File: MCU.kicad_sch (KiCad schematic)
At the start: 41 parts, among them IC6 ATSAMD21G18A-MF, J10 Conn_01x10, J11 Conn_01x06, J7 Conn_01x08, J9 Conn_01x08, Q1 XTAL_32.768KHZ_ABRACON_ABS09-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

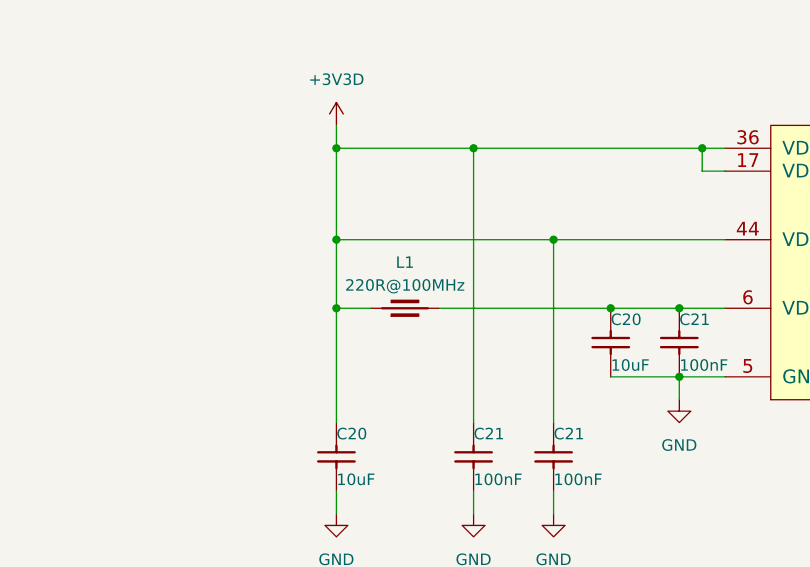
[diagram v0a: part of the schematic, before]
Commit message: Added input connector, switch, filtering and USB TVS
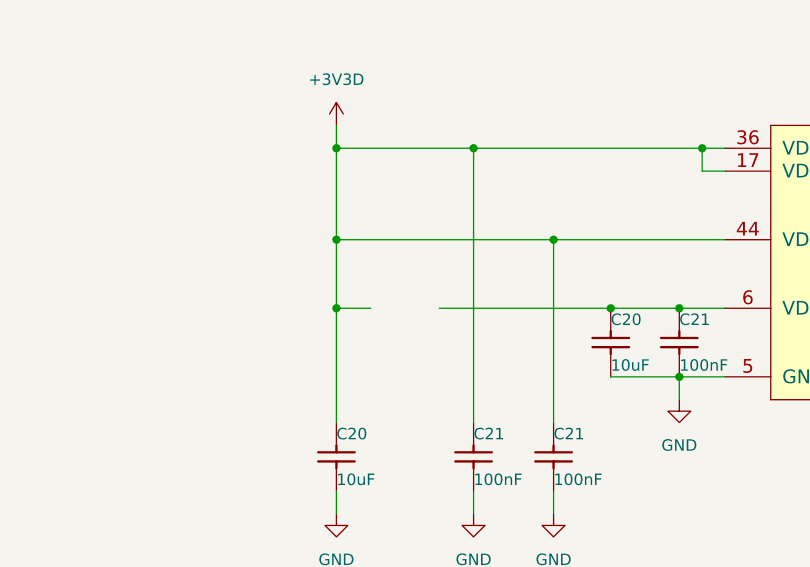
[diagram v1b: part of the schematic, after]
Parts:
- removed L1: IND0603_MURATA_BLM18SG221TN1, Inductors SMD:INDC1608X95N, symbol Inductors SMD:IND0603_MURATA_BLM18SG221TN1
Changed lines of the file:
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@@
-    )
-  )
-  (symbol (lib_id "Inductors SMD:IND0603_MURATA_BLM18SG221TN1") (at 99.06 214.63 0) (unit 1)
-    (in_bom yes) (on_board yes) (dnp no)
-    (property "Reference" "L1" (at 102.87 209.55 0)
-      (effects (font (size 1.27 1.27)))
-    )
-    (property "Value" "IND0603_MURATA_BLM18SG221TN1" (at 99.06 219.583 0)
-      (effects (font (size 1.27 1.27)) (justify left) hide)
-    )
-    (property "Footprint" "Inductors SMD:INDC1608X95N" (at 99.06 221.488 0)
-      (effects (font (size 1.27 1.27)) (justify left) hide)
-    )
-    (property "Datasheet" "\\\\cern.ch\\dfs\\Applications\\Altium\\Datasheets\\IND0603_MURATA_BLM18S.pdf" (at 99.06 223.393 0)
-      (effects (font (size 1.27 1.27)) (justify left) hide)
-    )
-    (property "Val" "220R@100MHz" (at 102.87 212.09 0)
-      (effects (font (size 1.27 1.27)))
-    )
-    (property "Part Number" "IND0603_MURATA_BLM18SG221TN1" (at 99.06 225.298 0)
-      (effects (font (size 1.27 1.27)) (justify left) hide)
-    )
-    (property "Library Ref" "Ferrite Bead" (at 99.06 227.203 0)
-      (effects (font (size 1.27 1.27)) (justify left) hide)
-    )
-    (property "Library Path" "SchLib\\Inductors & Transformers.SchLib" (at 99.06 229.108 0)
-      (effects (font (size 1.27 1.27)) (justify left) hide)
-    )
-    (property "Comment" "220R@100MHz" (at 99.06 231.013 0)
-      (effects (font (size 1.27 1.27)) (justify left) hide)
-    )
-    (property "Component Kind" "Standard" (at 99.06 232.918 0)
-      (effects (font (size 1.27 1.27)) (justify left) hide)
-    )
-    (property "Component Type" "Standard" (at 99.06 234.823 0)
-      (effects (font (size 1.27 1.27)) (justify left) hide)
-    )
-    (property "PackageDescription" " " (at 99.06 236.728 0)
-      (effects (font (size 1.27 1.27)) (justify left) hide)
-    )
-    (property "Pin Count" "2" (at 99.06 238.633 0)
-      (effects (font (size 1.27 1.27)) (justify left) hide)
-    )
-    (property "Footprint Path" "PcbLib\\Inductors SMD.PcbLib" (at 99.06 240.538 0)
-      (effects (font (size 1.27 1.27)) (justify left) hide)
-    )
-    (property "Footprint Ref" "INDC1608X95N" (at 99.06 242.443 0)
-      (effects (font (size 1.27 1.27)) (justify left) hide)
-    )
-    (property "Status" " " (at 99.06 244.348 0)
-      (effects (font (size 1.27 1.27)) (justify left) hide)
-    )
-    (property "Power" "2.5A" (at 99.06 246.253 0)
-      (effects (font (size 1.27 1.27)) (justify left) hide)
-    )
-    (property "Resistance" "0.04R" (at 99.06 248.158 0)
-      (effects (font (size 1.27 1.27)) (justify left) hide)
-    )
-    (property "Tolerance" "±25%" (at 99.06 250.063 0)
-      (effects (font (size 1.27 1.27)) (justify left) hide)
-    )
-    (property "Part Description" "SMD EMIFIL Suppression Chip Ferrite Bead" (at 99.06 251.968 0)
-      (effects (font (size 1.27 1.27)) (justify left) hide)
-    )
-    (property "Manufacturer" "MURATA" (at 99.06 253.873 0)
-      (effects (font (size 1.27 1.27)) (justify left) hide)
-    )
-    (property "Manufacturer Part Number" "BLM18SG221TN1" (at 99.06 255.778 0)
-      (effects (font (size 1.27 1.27)) (justify left) hide)
-    )
-    (property "Case" "0603" (at 99.06 257.683 0)
-      (effects (font (size 1.27 1.27)) (justify left) hide)
-    )
-    (property "Mounted" "Yes" (at 99.06 259.588 0)
-      (effects (font (size 1.27 1.27)) (justify left) hide)
-    )
-    (property "Socket" "No" (at 99.06 261.493 0)
-      (effects (font (size 1.27 1.27)) (justify left) hide)
-    )
-    (property "SMD" "Yes" (at 99.06 263.398 0)
-      (effects (font (size 1.27 1.27)) (justify left) hide)
-    )
-    (property "Sense Comment" " " (at 99.06 265.303 0)
-      (effects (font (size 1.27 1.27)) (justify left) hide)
-    )
-    (property "Sense" "No" (at 99.06 267.208 0)
-      (effects (font (size 1.27 1.27)) (justify left) hide)
-    )
-    (property "Status Comment" " " (at 99.06 269.113 0)
-      (effects (font (size 1.27 1.27)) (justify left) hide)
-    )
-    (property "ComponentHeight" "0.95mm" (at 99.06 271.018 0)
-      (effects (font (size 1.27 1.27)) (justify left) hide)
-    )
-    (property "HelpURL" "\\\\cern.ch\\dfs\\Applications\\Altium\\Datasheets\\IND0603_MURATA_BLM18S.pdf" (at 99.06 272.923 0)
-      (effects (font (size 1.27 1.27)) (justify left) hide)
-    )
-    (property "Author" "CERN DEM MR" (at 99.06 274.828 0)
-      (effects (font (size 1.27 1.27)) (justify left) hide)
-    )
-    (property "CreateDate" "01/08/16 00:00:00" (at 99.06 276.733 0)
-      (effects (font (size 1.27 1.27)) (justify left) hide)
-    )
-    (property "LatestRevisionDate" "10/25/18 00:00:00" (at 99.06 278.638 0)
-      (effects (font (size 1.27 1.27)) (justify left) hide)
-    )
-    (property "Database Table Name" "Inductors & Transformers" (at 99.06 280.543 0)
-      (effects (font (size 1.27 1.27)) (justify left) hide)
-    )
-    (property "Library Name" "Inductors SMD" (at 99.06 282.448 0)
-      (effects (font (size 1.27 1.27)) (justify left) hide)
-    )
-    (property "Footprint Library" "Inductors SMD" (at 99.06 284.353 0)
-      (effects (font (size 1.27 1.27)) (justify left) hide)
-    )
-    (property "License" "This work is licensed under the Creative Commons CC-BY-SA 4.0 License. To the extent that circuit schematics that use Licensed Material can be considered to be ‘Adapted Material’, then the copyright holder waives article 3.b of the license with respect to these schematics." (at 99.06 286.258 0)
-      (effects (font (size 1.27 1.27)) (justify left) hide)
-    )
-    (pin "1")
-    (pin "2")
-    (instances
-      (project "Accurate_Eval"
-        (path "/d3b6a045-fd77-42ad-b330-1b1925488537/c6a8b2ea-c0f0-4c02-aeaa-57ac874f0dd5"
-          (reference "L1") (unit 1)
-        )
-      )
     )
   )

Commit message: Reannotated schematic, added PSU calculation, some polish
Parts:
- added L2: IND0603_MURATA_BLM18SG221TN1, Inductors SMD:INDC1608X95N, symbol Inductors SMD:IND0603_MURATA_BLM18SG221TN1
- renumbered C82 to C32, C83 to C33, C77 to C39, C21 to C?, C20 to C?, IC6 to IC8, J9 to J6, J10 to J7, J7 to J8, J11 to J9, LD2 to LD?, LD3 to LD?, LD5 to LD?, LD13 to LD?, PB1 to PB?, R47 to R18, R44 to R19, R50 to R20, R45 to R21, R42 to R23, R43 to R24, R37 to R?, R32 to R?, R38 to R?, R20 to R?, TP4 to TP?
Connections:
- net +3V3D: now also L2.1
- net at C?.1, C?.1, IC8.6 (VDDANA): now also L2.2

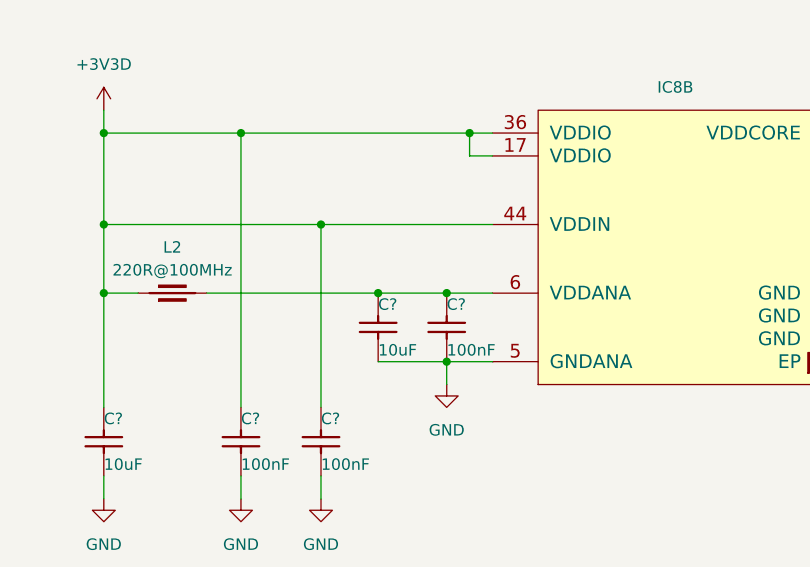
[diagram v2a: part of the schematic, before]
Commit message: Added USB connector, EEPROM, and replaced 2V5 diode
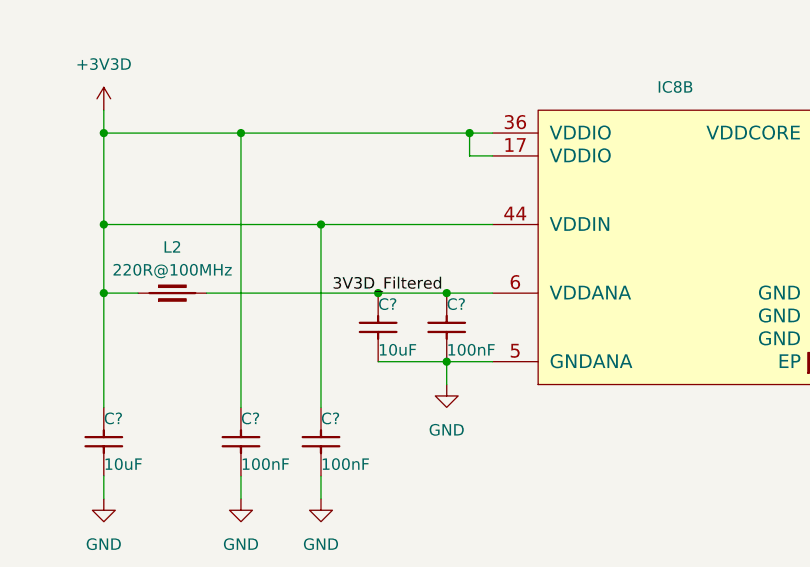
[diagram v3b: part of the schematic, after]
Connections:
- net 3V3D_Filtered: now reaches C?.1, C?.1, IC8.6 (VDDANA), L2.2
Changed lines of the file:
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@@
+    (effects (font (size 1.27 1.27)) (justify left bottom))
+  )
+  (label "3V3D_Filtered" (at 120.65 214.63 0) (fields_autoplaced)
     (effects (font (size 1.27 1.27)) (justify left bottom))
   )

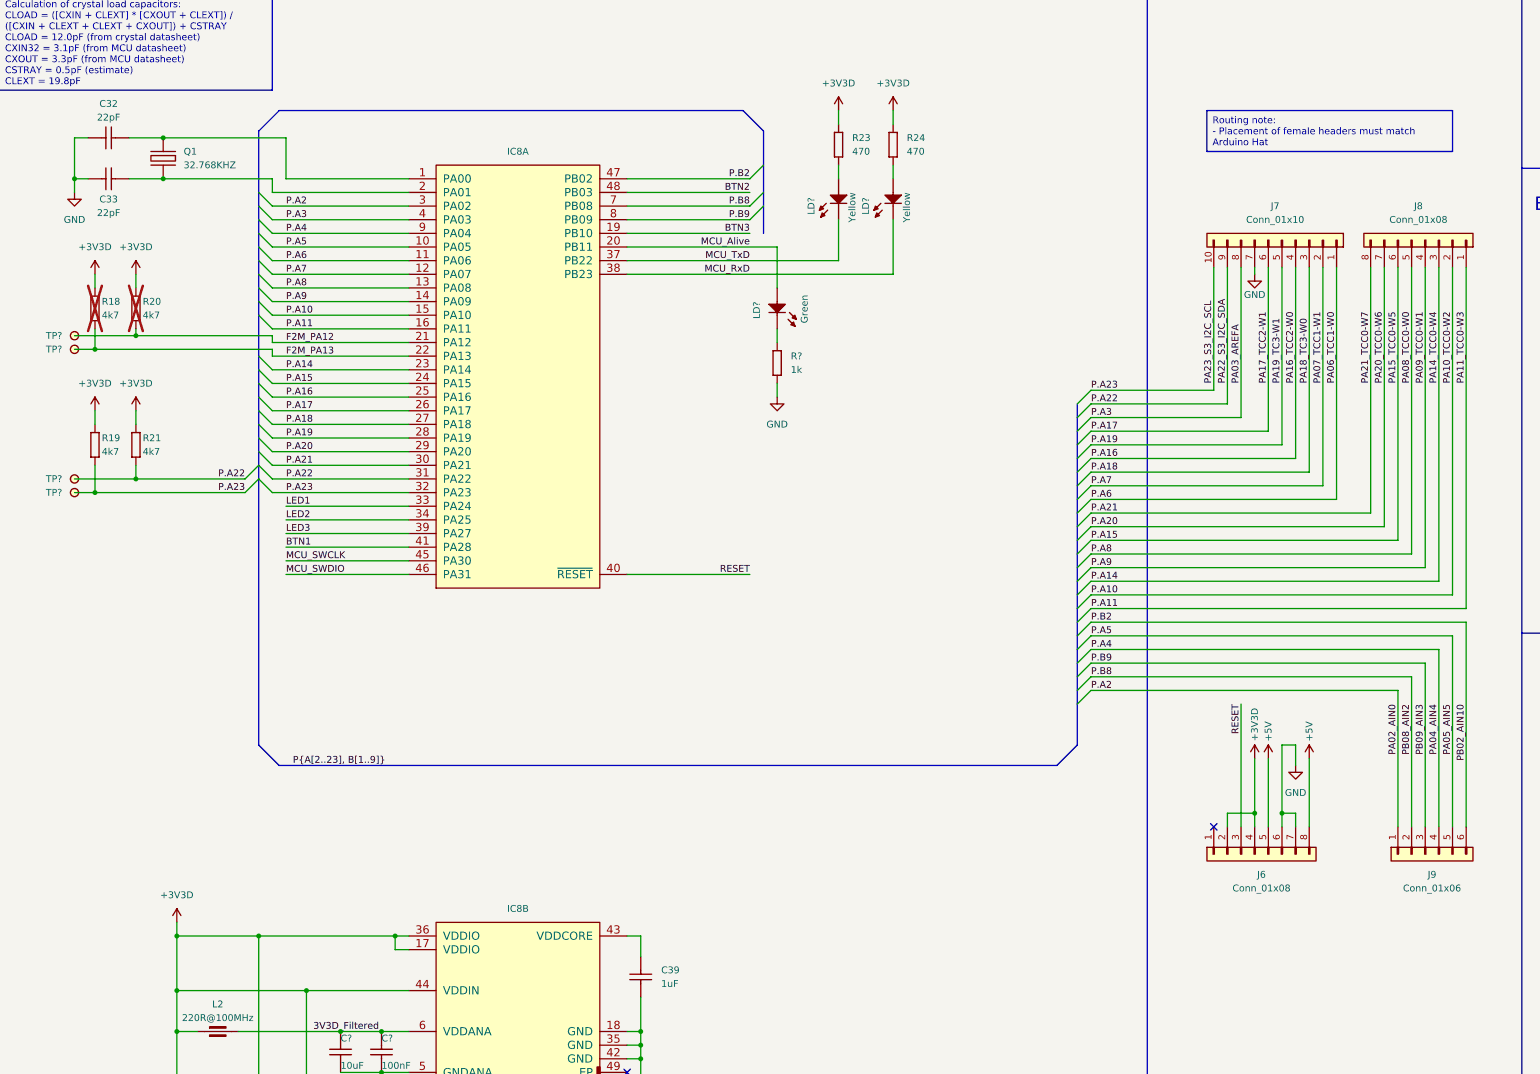
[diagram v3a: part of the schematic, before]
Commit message: Added OTA ADC
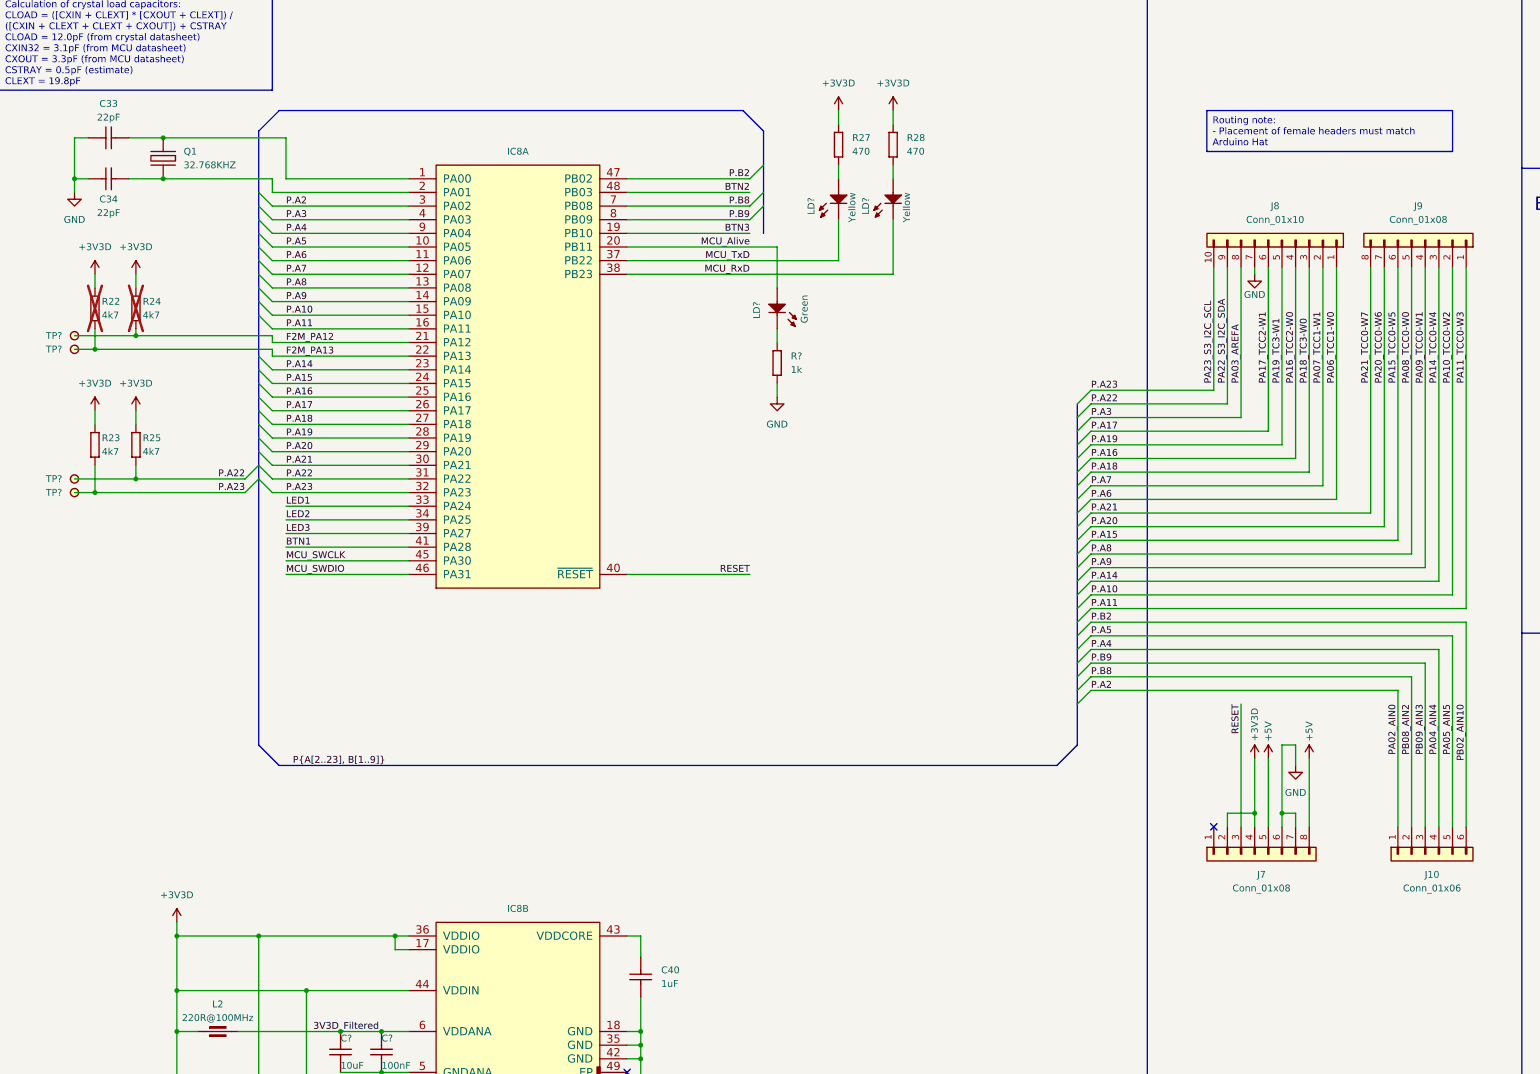
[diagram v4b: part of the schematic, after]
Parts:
- renumbered C32 to C33, C33 to C34, C39 to C40, J9 to J10, J6 to J7, J7 to J8, J8 to J9, R18 to R22, R19 to R23, R20 to R24, R21 to R25, R23 to R27, R24 to R28
